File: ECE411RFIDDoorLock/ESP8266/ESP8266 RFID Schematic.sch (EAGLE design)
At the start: 31 parts, among them J4 1050170001, M1 SERVO, Q3 MMBT2222ALT1GOSCT-ND, T1 600mA/40V, T2 600mA/40V, U1 CP2104, U2 AP2112K-3.3TRG1, X1 ESP-12E

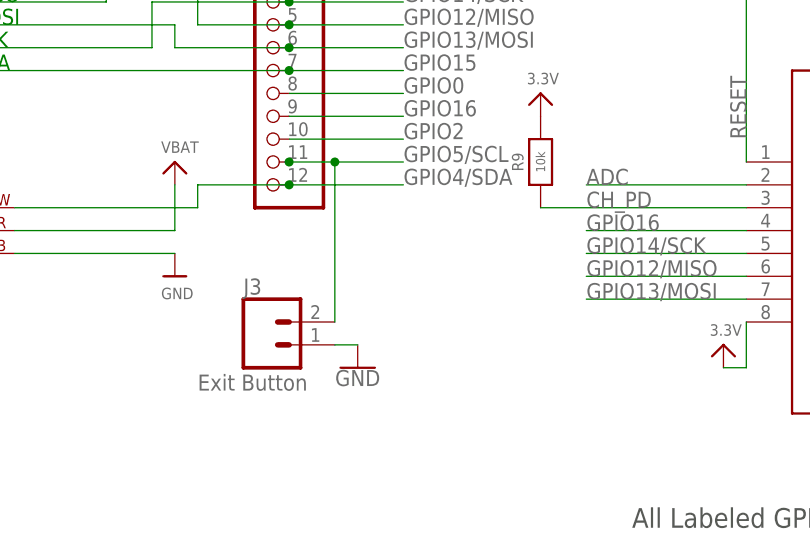
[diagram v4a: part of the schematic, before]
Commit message: Added pull up resistor to push to exit
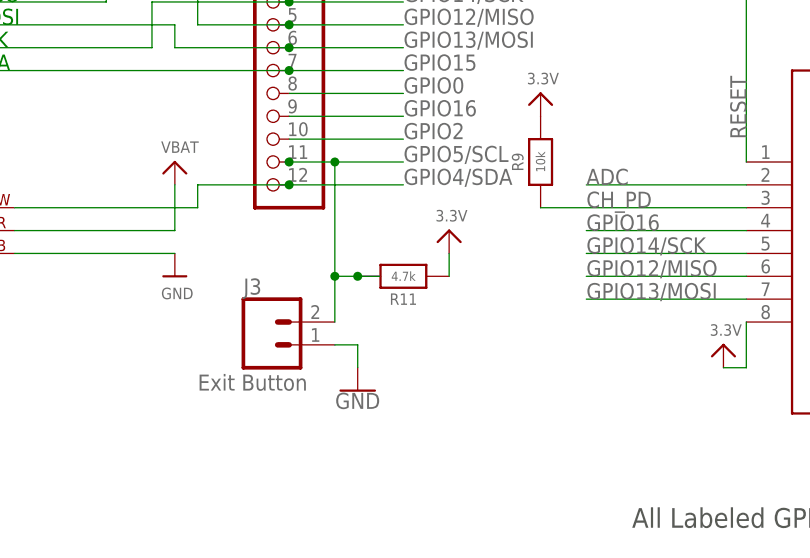
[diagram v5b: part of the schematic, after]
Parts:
- added R11: 4.7k, microbuilder:RESISTOR0603MINI
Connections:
- net 3.3V: now also R11.1
- net GPIO5/SCL: now also R11.2
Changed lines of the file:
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@@
 <part name="S1" library="B3S-1000" deviceset="B3S-1000" device=""/>
 <part name="U2" library="AP2112K-3.3TRG1" deviceset="AP2112K-3.3TRG1" device=""/>
+<part name="R11" library="microbuilder" deviceset="RESISTOR" device="0603MINI" value="4.7k"/>
+<part name="U$18" library="microbuilder" deviceset="3.3V" device=""/>
 </parts>
 <sheets>
@@
 <attribute name="VALUE" x="216.916" y="59.436" size="1.27" layer="96"/>
 </instance>
-<instance part="GND13" gate="1" x="76.2" y="22.86" smashed="yes">
-<attribute name="VALUE" x="76.2" y="22.606" size="1.778" layer="96" align="top-center"/>
+<instance part="GND13" gate="1" x="76.2" y="20.32" smashed="yes">
+<attribute name="VALUE" x="76.2" y="20.066" size="1.778" layer="96" align="top-center"/>
 </instance>
 <instance part="J2" gate="G$1" x="55.88" y="121.92" smashed="yes">
@@
 <attribute name="NAME" x="58.37705" y="112.787609375" size="2.08946875" layer="95" ratio="10" rot="SR0"/>
 <attribute name="VALUE" x="55.8511" y="92.4893" size="2.0883" layer="96" ratio="10" rot="SR0"/>
+</instance>
+<instance part="R11" gate="G$1" x="81.28" y="33.02" smashed="yes" rot="R180">
+<attribute name="NAME" x="81.28" y="30.48" size="1.27" layer="95" font="vector" rot="R180" align="center"/>
+<attribute name="VALUE" x="81.28" y="33.02" size="1.016" layer="96" font="vector" ratio="15" rot="R180" align="center"/>
+</instance>
+<instance part="U$18" gate="G$1" x="86.36" y="38.1" smashed="yes">
+<attribute name="VALUE" x="84.836" y="39.116" size="1.27" layer="96"/>
 </instance>
 </instances>
@@
 </segment>
 <segment>
-<pinref part="J3" gate="G$1" pin="1"/>
-<pinref part="GND13" gate="1" pin="GND"/>
-<wire x1="73.66" y1="25.4" x2="76.2" y2="25.4" width="0.1524" layer="91"/>
-</segment>
-<segment>
 <pinref part="GND11" gate="1" pin="GND"/>
 <pinref part="R8" gate="G$1" pin="1"/>
@@
 <wire x1="78.74" y1="99.06" x2="81.28" y2="99.06" width="0.1524" layer="91"/>
 <wire x1="81.28" y1="99.06" x2="81.28" y2="91.44" width="0.1524" layer="91"/>
+</segment>
+<segment>
+<pinref part="J3" gate="G$1" pin="1"/>
+<pinref part="GND13" gate="1" pin="GND"/>
+<wire x1="73.66" y1="25.4" x2="76.2" y2="25.4" width="0.1524" layer="91"/>
+<wire x1="76.2" y1="25.4" x2="76.2" y2="22.86" width="0.1524" layer="91"/>
 </segment>
 </net>
@@
 <wire x1="73.66" y1="45.72" x2="81.28" y2="45.72" width="0.1524" layer="91"/>
 <wire x1="68.58" y1="45.72" x2="73.66" y2="45.72" width="0.1524" layer="91"/>
-<wire x1="73.66" y1="45.72" x2="73.66" y2="27.94" width="0.1524" layer="91"/>
+<wire x1="73.66" y1="45.72" x2="73.66" y2="33.02" width="0.1524" layer="91"/>
 <junction x="68.58" y="45.72"/>
 <pinref part="J3" gate="G$1" pin="2"/>
 <junction x="73.66" y="45.72"/>
+<wire x1="73.66" y1="33.02" x2="73.66" y2="27.94" width="0.1524" layer="91"/>
+<wire x1="76.2" y1="33.02" x2="78.6638" y2="33.02" width="0.1524" layer="91"/>
+<pinref part="R11" gate="G$1" pin="2"/>
+<wire x1="76.2" y1="33.02" x2="73.66" y2="33.02" width="0.1524" layer="91"/>
+<junction x="76.2" y="33.02"/>
+<junction x="73.66" y="33.02"/>
 </segment>
 </net>
@@
 <pinref part="U$12" gate="G$1" pin="3.3V"/>
 </segment>
-</net>
+<segment>
+<pinref part="U$18" gate="G$1" pin="3.3V"/>
+<pinref part="R11" gate="G$1" pin="1"/>
+<wire x1="86.36" y1="35.56" x2="86.36" y2="33.02" width="0.1524" layer="91"/>
+</segment>
+</net>
